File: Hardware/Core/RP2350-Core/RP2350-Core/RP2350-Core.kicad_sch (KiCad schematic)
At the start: 0 parts

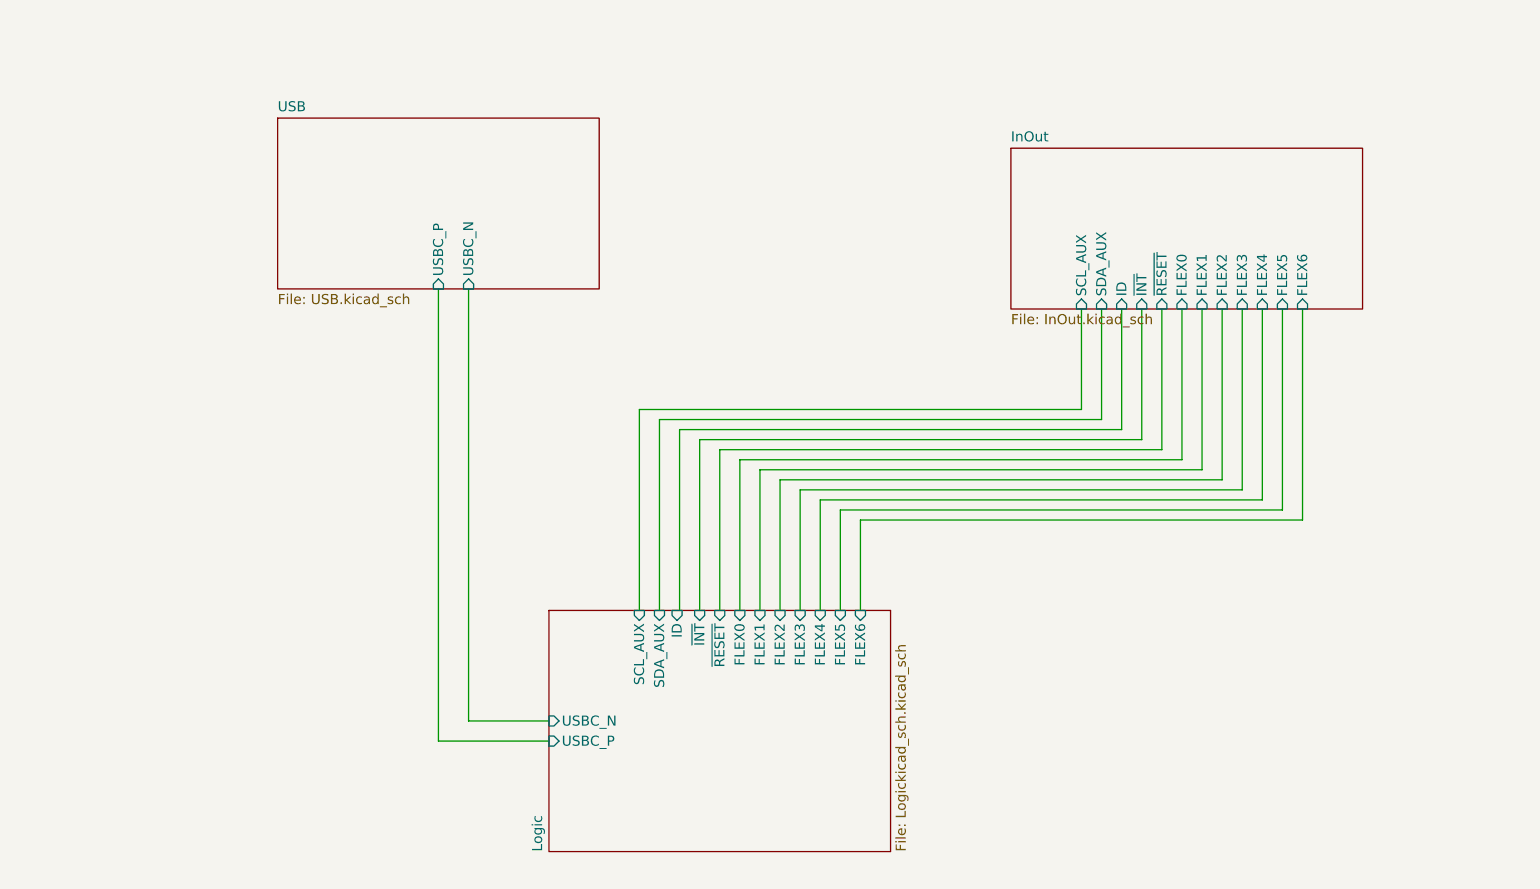
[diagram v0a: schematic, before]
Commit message: Add expansion connector
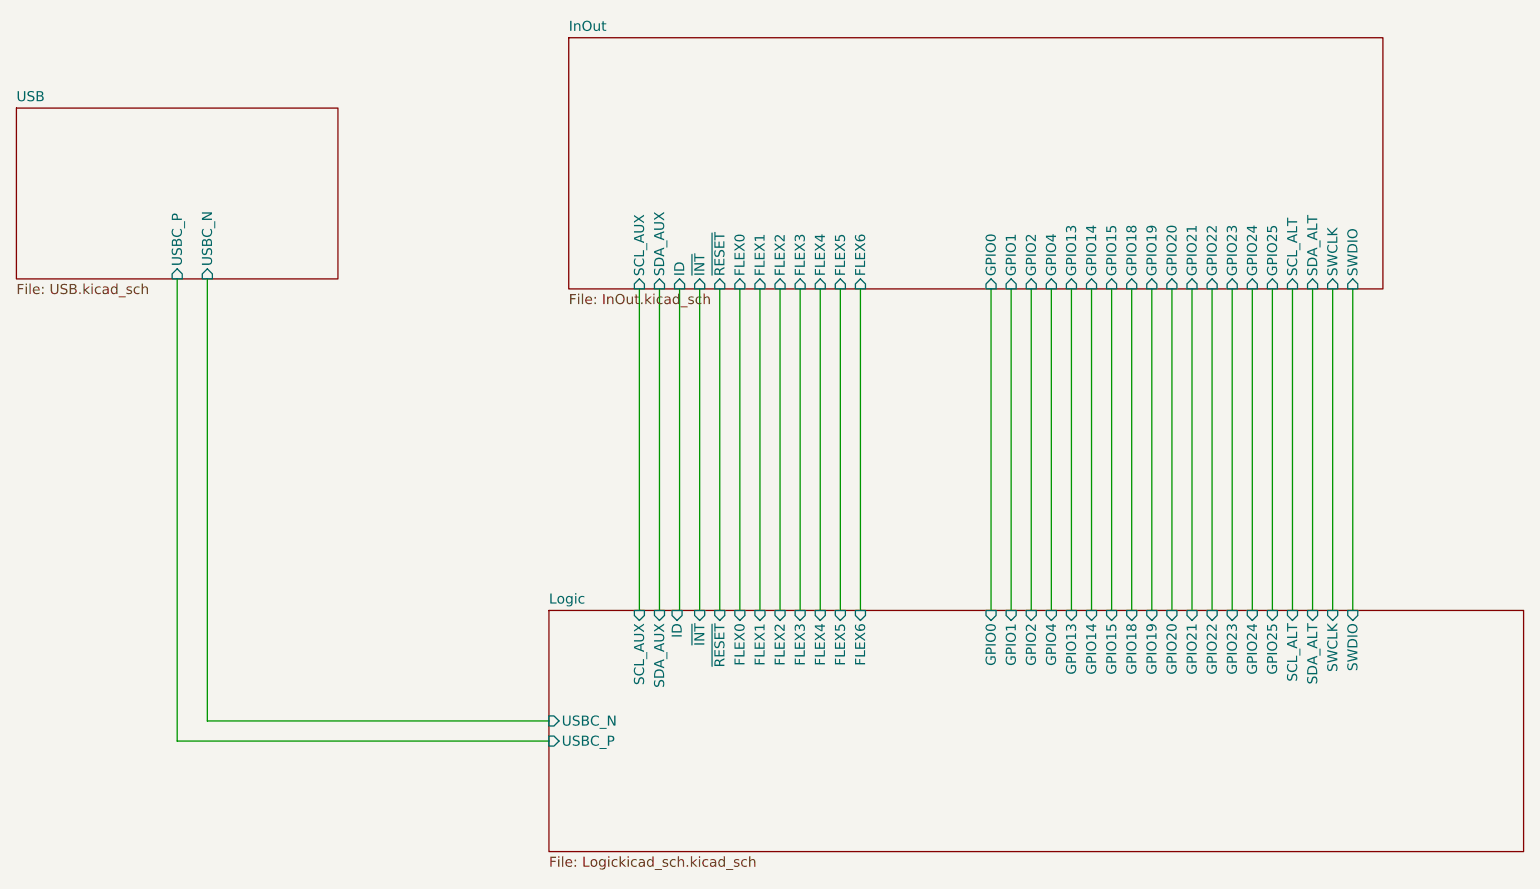
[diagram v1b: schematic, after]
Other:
- sheet InOut ports: added GPIO0, GPIO1, GPIO13, GPIO14, GPIO15, GPIO18, GPIO19, GPIO2, GPIO20, GPIO21, GPIO22, GPIO23, GPIO24, GPIO25, GPIO4, SCL_ALT, SDA_ALT, SWCLK, SWDIO; removed none
- sheet Logic ports: added GPIO0, GPIO1, GPIO13, GPIO14, GPIO15, GPIO18, GPIO19, GPIO2, GPIO20, GPIO21, GPIO22, GPIO23, GPIO24, GPIO25, GPIO4, SCL_ALT, SDA_ALT, SWCLK, SWDIO; removed none
